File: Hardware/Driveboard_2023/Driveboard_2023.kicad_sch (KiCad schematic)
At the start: 64 parts

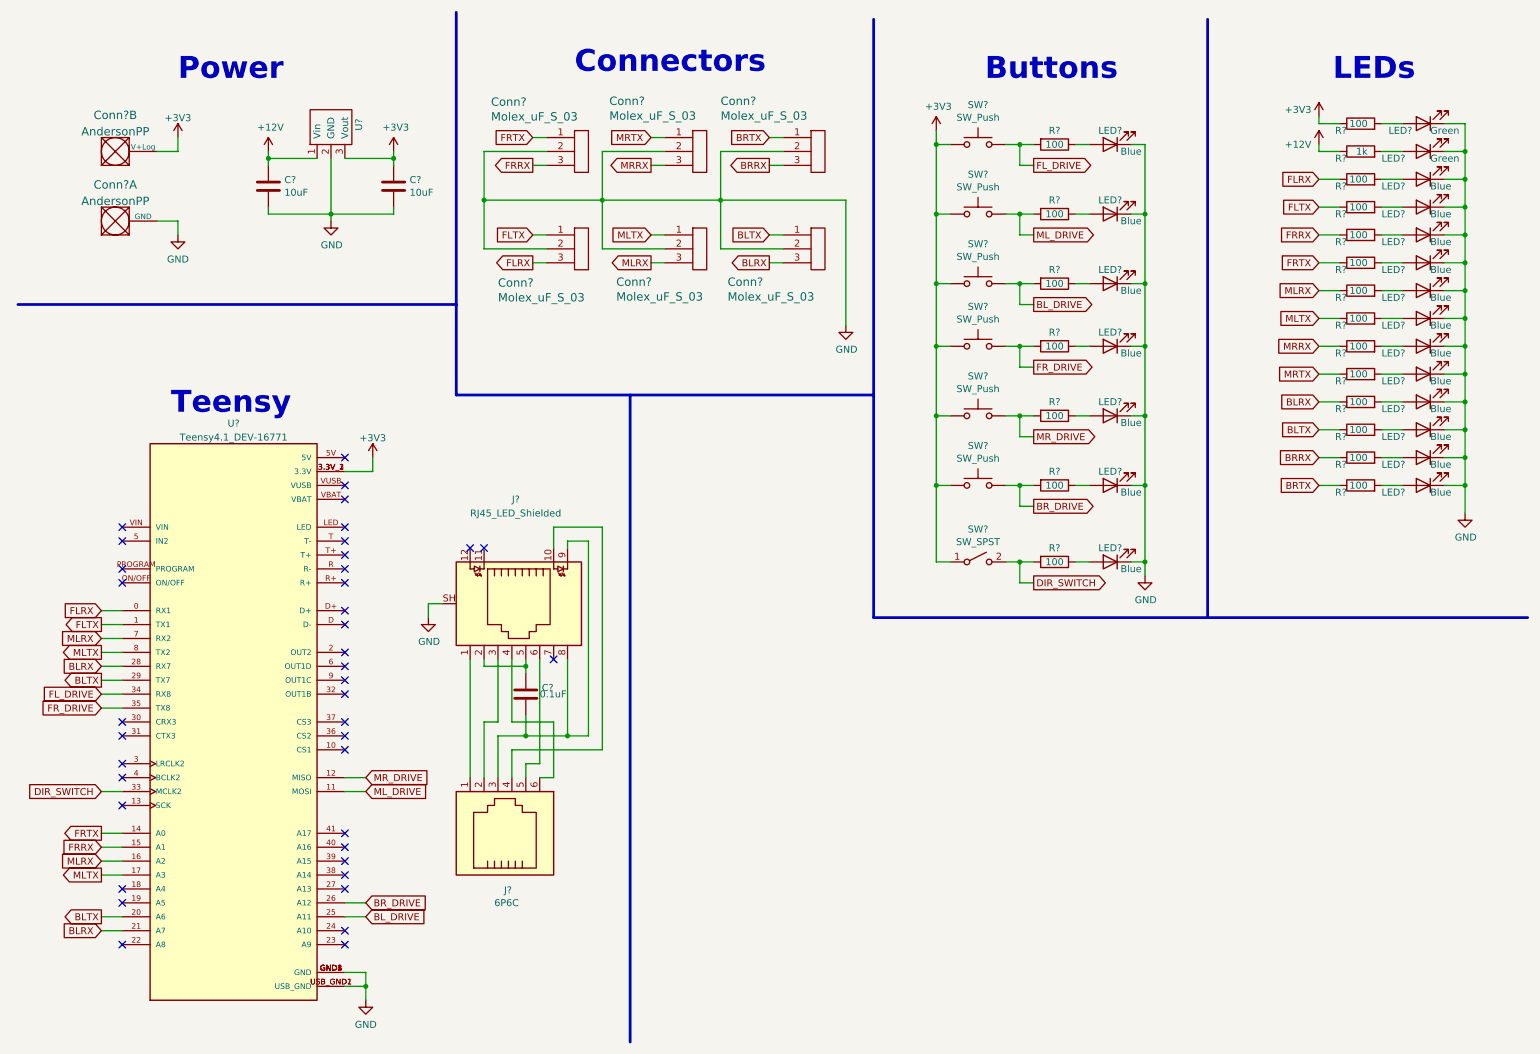
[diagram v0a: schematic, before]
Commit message: Fixed Changes
Changed 12V to 36V, same thing with OKI from TSR
Changed switch to a 2 position switch
Changed 12V LED to 36V and add 3k Resistor
Changed all Rx LED to Yellow
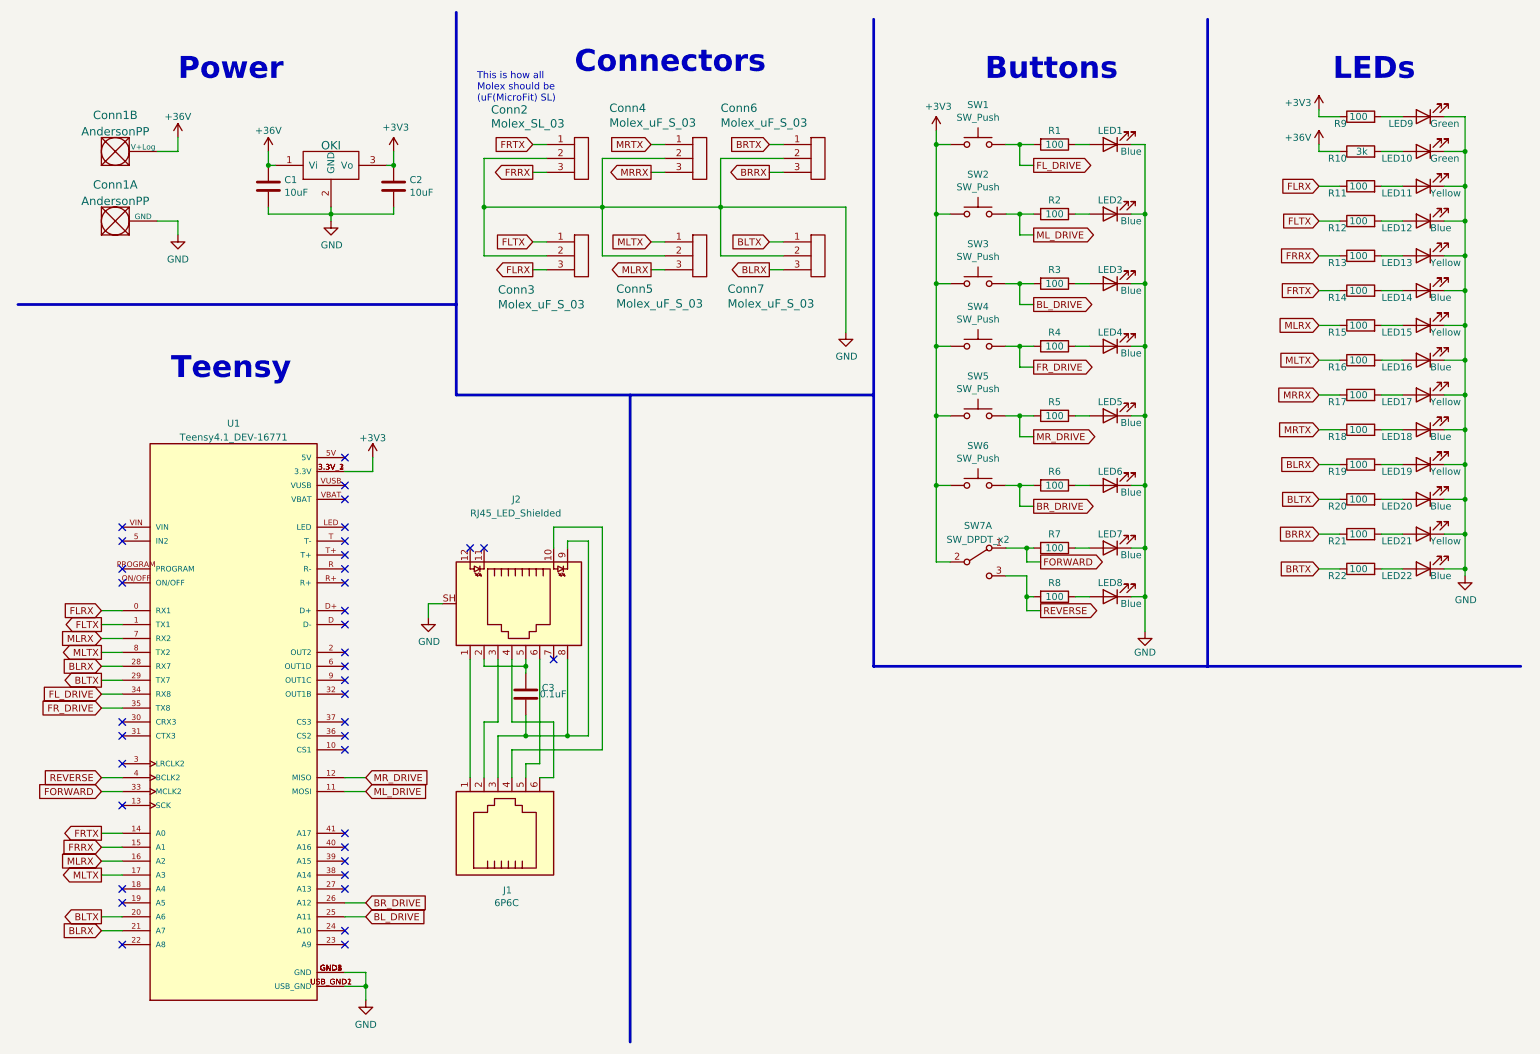
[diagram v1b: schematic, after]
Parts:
- removed Conn?: Molex_uF_S_03, MRDT_Connectors:MOLEX_uF_S_03_Horizontal, symbol MRDT_Connectors:Molex_uF_S_03
- removed SW?: SW_SPST, Button_Switch_THT:SW_Slide_1P2T_CK_OS102011MS2Q, symbol Switch:SW_SPST
- removed U?: TSR1-2433, MRDT_Devices:TSR_1-2433, symbol Driveboard_2022-rescue:TSR1-2433-MRDT_Devices
- added Conn2: Molex_SL_03, symbol MRDT_Connectors:Molex_SL_03
- added LED8: Blue, LED_SMD:LED_0603_1608Metric_Pad1.05x0.95mm_HandSolder, symbol Device:LED
- added R8: 100, Resistor_SMD:R_0603_1608Metric_Pad0.98x0.95mm_HandSolder, symbol Device:R
- added SW7: SW_DPDT_x2, symbol Switch:SW_DPDT_x2
- added U2: OKI, symbol MRDT_Devices:OKI
- LED11, LED13, LED15, LED17, LED19, LED21: renamed from LED?; value Blue -> Yellow
- R10: renamed from R?; value 1k -> 3k
- U1: renamed from U?; footprint MODULE_DEV-16771 -> MRDT_Shields:MODULE_DEV-16771
- gave numbers to parts that had none: 52
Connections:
- net +3V3: now also SW7.2 (B), U2.3 (Vo); no longer Conn1.2 (V+Log)
- net FRRX: now also Conn2.3
- net FRTX: now also Conn2.1
- net GND: now also Conn2.2, LED8.1 (K), U2.2 (GND)
- net REVERSE: now reaches U1.4 (BCLK2)
- net REVERSE: now also R8.2, SW7.3 (C)
- net +12V renamed +36V
- net +36V: now also Conn1.2 (V+Log), U2.1 (Vi)
- net DIR_SWITCH renamed FORWARD
- net FORWARD: now also SW7.1 (A)
- new net: LED8.2 (A), R8.1
- no-connect marks 39 -> 38
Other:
- note added: "This is how all Molex should be (uF(MicroFit) SL)"
- moved on the sheet: Conn3, Conn4, Conn5, Conn6, Conn7, LED11, LED12, LED13, LED14, LED15, LED16, LED17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

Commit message: Microfit to SL
Changed microfits to SL
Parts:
- removed Conn3, Conn4, Conn5, Conn6, Conn7: Molex_uF_S_03, MRDT_Connectors:MOLEX_uF_S_03_Horizontal, symbol MRDT_Connectors:Molex_uF_S_03
- added Conn? (x5): Molex_SL_03, symbol MRDT_Connectors:Molex_SL_03
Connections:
- net BLRX: now also Conn?.3
- net BLTX: now also Conn?.1
- net BRRX: now also Conn?.3
- net BRTX: now also Conn?.1
- net FLRX: now also Conn?.3
- net FLTX: now also Conn?.1
- net GND: now also Conn?.2, Conn?.2, Conn?.2, Conn?.2, Conn?.2
- net MLRX: now also Conn?.3
- net MLTX: now also Conn?.1
- net MRRX: now also Conn?.3
- net MRTX: now also Conn?.1
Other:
- note removed: "This is how all Molex should be (uF(MicroFit) SL)"
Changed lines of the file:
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@@
     (effects (font (size 4 4) (thickness 0.8) bold) (justify left bottom))
-  )
-  (text "This is how all \nMolex should be \n(uF(MicroFit) SL)"
-    (at 93.98 26.67 0)
-    (effects (font (size 1.27 1.27)) (justify left bottom))
   )
   (text "LEDs" (at 250.19 22.86 0)
@@
     (pin "1")
   )
+  (symbol (lib_id "MRDT_Connectors:Molex_SL_03") (at 133.35 40.64 0) (unit 1)
+    (in_bom yes) (on_board yes)
+    (property "Reference" "Conn?" (id 0) (at 118.11 27.94 0)
+      (effects (font (size 1.524 1.524)) (justify left))
+    )
+    (property "Value" "Molex_SL_03" (id 1) (at 118.11 30.48 0)
+      (effects (font (size 1.524 1.524)) (justify left))
+    )
+    (property "Footprint" "" (id 2) (at 133.35 40.64 0)
+      (effects (font (size 1.524 1.524)) hide)
+    )
+    (property "Datasheet" "" (id 3) (at 133.35 40.64 0)
+      (effects (font (size 1.524 1.524)) hide)
+    )
+    (pin "1")
+    (pin "2")
+    (pin "3")
+  )
+  (symbol (lib_id "MRDT_Connectors:Molex_SL_03") (at 154.94 58.42 0) (unit 1)
+    (in_bom yes) (on_board yes)
+    (property "Reference" "Conn?" (id 0) (at 139.7 60.96 0)
+      (effects (font (size 1.524 1.524)) (justify left))
+    )
+    (property "Value" "Molex_SL_03" (id 1) (at 139.7 63.5 0)
+      (effects (font (size 1.524 1.524)) (justify left))
+    )
+    (property "Footprint" "" (id 2) (at 154.94 58.42 0)
+      (effects (font (size 1.524 1.524)) hide)
+    )
+    (property "Datasheet" "" (id 3) (at 154.94 58.42 0)
+      (effects (font (size 1.524 1.524)) hide)
+    )
+    (pin "1")
+    (pin "2")
+    (pin "3")
+  )
   (symbol (lib_id "Device:R") (at 199.39 59.69 270) (unit 1)
     (in_bom yes) (on_board yes)
@@
     (pin "1")
     (pin "2")
-  )
-  (symbol (lib_id "MRDT_Connectors:Molex_uF_S_03") (at 154.94 40.64 0) (unit 1)
-    (in_bom yes) (on_board yes)
-    (property "Reference" "Conn6" (id 0) (at 138.43 27.6352 0)
-      (effects (font (size 1.524 1.524)) (justify left))
-    )
-    (property "Value" "Molex_uF_S_03" (id 1) (at 138.43 30.3276 0)
-      (effects (font (size 1.524 1.524)) (justify left))
-    )
-    (property "Footprint" "MRDT_Connectors:MOLEX_uF_S_03_Horizontal" (id 2) (at 154.94 40.64 0)
-      (effects (font (size 1.524 1.524)) hide)
-    )
-    (property "Datasheet" "" (id 3) (at 154.94 40.64 0)
-      (effects (font (size 1.524 1.524)) hide)
-    )
-    (pin "1")
-    (pin "2")
-    (pin "3")
   )
   (symbol (lib_id "Device:LED") (at 266.7 60.96 180) (unit 1)
@@
     )
     (pin "1")
+  )
+  (symbol (lib_id "MRDT_Connectors:Molex_SL_03") (at 111.76 58.42 0) (unit 1)
+    (in_bom yes) (on_board yes)
+    (property "Reference" "Conn?" (id 0) (at 96.52 60.96 0)
+      (effects (font (size 1.524 1.524)) (justify left))
+    )
+    (property "Value" "Molex_SL_03" (id 1) (at 96.52 63.5 0)
+      (effects (font (size 1.524 1.524)) (justify left))
+    )
+    (property "Footprint" "" (id 2) (at 111.76 58.42 0)
+      (effects (font (size 1.524 1.524)) hide)
+    )
+    (property "Datasheet" "" (id 3) (at 111.76 58.42 0)
+      (effects (font (size 1.524 1.524)) hide)
+    )
+    (pin "1")
+    (pin "2")
+    (pin "3")
   )
   (symbol (lib_id "Device:R") (at 199.39 71.12 270) (unit 1)
@@
     (pin "VUSB")
   )
-  (symbol (lib_id "MRDT_Connectors:Molex_uF_S_03") (at 133.35 58.42 0) (unit 1)
-    (in_bom yes) (on_board yes)
-    (property "Reference" "Conn5" (id 0) (at 119.38 60.6552 0)
-      (effects (font (size 1.524 1.524)) (justify left))
-    )
-    (property "Value" "Molex_uF_S_03" (id 1) (at 119.38 63.3476 0)
-      (effects (font (size 1.524 1.524)) (justify left))
-    )
-    (property "Footprint" "MRDT_Connectors:MOLEX_uF_S_03_Horizontal" (id 2) (at 133.35 58.42 0)
-      (effects (font (size 1.524 1.524)) hide)
-    )
-    (property "Datasheet" "" (id 3) (at 133.35 58.42 0)
-      (effects (font (size 1.524 1.524)) hide)
-    )
-    (pin "1")
-    (pin "2")
-    (pin "3")
-  )
   (symbol (lib_id "Device:R") (at 255.27 41.91 90) (unit 1)
     (in_bom yes) (on_board yes)
@@
     (pin "1")
     (pin "2")
+  )
+  (symbol (lib_id "MRDT_Connectors:Molex_SL_03") (at 154.94 40.64 0) (unit 1)
+    (in_bom yes) (on_board yes)
+    (property "Reference" "Conn?" (id 0) (at 139.7 27.94 0)
+      (effects (font (size 1.524 1.524)) (justify left))
+    )
+    (property "Value" "Molex_SL_03" (id 1) (at 139.7 30.48 0)
+      (effects (font (size 1.524 1.524)) (justify left))
+    )
+    (property "Footprint" "" (id 2) (at 154.94 40.64 0)
+      (effects (font (size 1.524 1.524)) hide)
+    )
+    (property "Datasheet" "" (id 3) (at 154.94 40.64 0)
+      (effects (font (size 1.524 1.524)) hide)
+    )
+    (pin "1")
+    (pin "2")
+    (pin "3")
   )
   (symbol (lib_id "Device:R") (at 255.27 48.26 90) (unit 1)
@@
     (pin "2")
   )
+  (symbol (lib_id "MRDT_Connectors:Molex_SL_03") (at 133.35 58.42 0) (unit 1)
+    (in_bom yes) (on_board yes)
+    (property "Reference" "Conn?" (id 0) (at 118.11 60.96 0)
+      (effects (font (size 1.524 1.524)) (justify left))
+    )
+    (property "Value" "Molex_SL_03" (id 1) (at 118.11 63.5 0)
+      (effects (font (size 1.524 1.524)) (justify left))
+    )
+    (property "Footprint" "" (id 2) (at 133.35 58.42 0)
+      (effects (font (size 1.524 1.524)) hide)
+    )
+    (property "Datasheet" "" (id 3) (at 133.35 58.42 0)
+      (effects (font (size 1.524 1.524)) hide)
+    )
+    (pin "1")
+    (pin "2")
+    (pin "3")
+  )
   (symbol (lib_id "Device:LED") (at 266.7 105.41 180) (unit 1)
     (in_bom yes) (on_board yes)
@@
     (pin "2")
   )
-  (symbol (lib_id "MRDT_Connectors:Molex_uF_S_03") (at 154.94 58.42 0) (unit 1)
-    (in_bom yes) (on_board yes)
-    (property "Reference" "Conn7" (id 0) (at 139.7 60.6552 0)
-      (effects (font (size 1.524 1.524)) (justify left))
-    )
-    (property "Value" "Molex_uF_S_03" (id 1) (at 139.7 63.3476 0)
-      (effects (font (size 1.524 1.524)) (justify left))
-    )
-    (property "Footprint" "MRDT_Connectors:MOLEX_uF_S_03_Horizontal" (id 2) (at 154.94 58.42 0)
-      (effects (font (size 1.524 1.524)) hide)
-    )
-    (property "Datasheet" "" (id 3) (at 154.94 58.42 0)
-      (effects (font (size 1.524 1.524)) hide)
-    )
-    (pin "1")
-    (pin "2")
-    (pin "3")
-  )
-  (symbol (lib_id "MRDT_Connectors:Molex_uF_S_03") (at 133.35 40.64 0) (unit 1)
-    (in_bom yes) (on_board yes)
-    (property "Reference" "Conn4" (id 0) (at 118.11 27.6352 0)
-      (effects (font (size 1.524 1.524)) (justify left))
-    )
-    (property "Value" "Molex_uF_S_03" (id 1) (at 118.11 30.3276 0)
-      (effects (font (size 1.524 1.524)) (justify left))
-    )
-    (property "Footprint" "MRDT_Connectors:MOLEX_uF_S_03_Horizontal" (id 2) (at 133.35 40.64 0)
-      (effects (font (size 1.524 1.524)) hide)
-    )
-    (property "Datasheet" "" (id 3) (at 133.35 40.64 0)
-      (effects (font (size 1.524 1.524)) hide)
-    )
-    (pin "1")
-    (pin "2")
-    (pin "3")
-  )
   (symbol (lib_id "Device:LED") (at 266.7 86.36 180) (unit 1)
     (in_bom yes) (on_board yes)
@@
     (pin "1")
     (pin "2")
-  )
-  (symbol (lib_id "MRDT_Connectors:Molex_uF_S_03") (at 111.76 58.42 0) (unit 1)
-    (in_bom yes) (on_board yes)
-    (property "Reference" "Conn3" (id 0) (at 97.79 60.8076 0)
-      (effects (font (size 1.524 1.524)) (justify left))
-    )
-    (property "Value" "Molex_uF_S_03" (id 1) (at 97.79 63.5 0)
-      (effects (font (size 1.524 1.524)) (justify left))
-    )
-    (property "Footprint" "MRDT_Connectors:MOLEX_uF_S_03_Horizontal" (id 2) (at 111.76 58.42 0)
-      (effects (font (size 1.524 1.524)) hide)
-    )
-    (property "Datasheet" "" (id 3) (at 111.76 58.42 0)
-      (effects (font (size 1.524 1.524)) hide)
-    )
-    (pin "1")
-    (pin "2")
-    (pin "3")
   )
   (symbol (lib_id "Connector:6P6C") (at 97.79 160.02 270) (mirror x) (unit 1)
@@
       (reference "Conn2") (unit 1) (value "Molex_SL_03") (footprint "")
     )
-    (path "/e98a6cb6-c539-46c8-a43e-716d478bcff1"
-      (reference "Conn3") (unit 1) (value "Molex_uF_S_03") (footprint "MRDT_Connectors:MOLEX_uF_S_03_Horizontal")
-    )
-    (path "/e2eff858-bafc-48bb-a76d-eaaabcaa951f"
-      (reference "Conn4") (unit 1) (value "Molex_uF_S_03") (footprint "MRDT_Connectors:MOLEX_uF_S_03_Horizontal")
-    )
-    (path "/7942e8c0-4de2-4bd1-9253-69ebfdb3526c"
-      (reference "Conn5") (unit 1) (value "Molex_uF_S_03") (footprint "MRDT_Connectors:MOLEX_uF_S_03_Horizontal")
-    )
-    (path "/2941794c-9d21-4e3b-bfbd-5d6e2ddf5873"
-      (reference "Conn6") (unit 1) (value "Molex_uF_S_03") (footprint "MRDT_Connectors:MOLEX_uF_S_03_Horizontal")
-    )
-    (path "/e1960e31-04f2-40e3-9802-306bee27948f"
-      (reference "Conn7") (unit 1) (value "Molex_uF_S_03") (footprint "MRDT_Connectors:MOLEX_uF_S_03_Horizontal")
+    (path "/1abc3be1-f403-48f4-8497-d62282d8dd47"
+      (reference "Conn?") (unit 1) (value "Molex_SL_03") (footprint "")
+    )
+    (path "/1e2f7b13-6f2b-4f36-a6ad-c884120f49ab"
+      (reference "Conn?") (unit 1) (value "Molex_SL_03") (footprint "")
+    )
+    (path "/65dd1fc9-0825-44f5-b231-bf2dd2fe6bc6"
+      (reference "Conn?") (unit 1) (value "Molex_SL_03") (footprint "")
+    )
+    (path "/84060289-6f0d-4cd3-891d-ed952d252733"
+      (reference "Conn?") (unit 1) (value "Molex_SL_03") (footprint "")
+    )
+    (path "/d7fd4eb9-0d60-438a-809c-ed65f8efa698"
+      (reference "Conn?") (unit 1) (value "Molex_SL_03") (footprint "")
     )
     (path "/eeeaa791-d0f1-4d41-a4cb-058952f69ac1"
